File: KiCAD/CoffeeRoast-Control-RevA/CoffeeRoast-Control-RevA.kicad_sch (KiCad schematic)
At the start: 0 parts

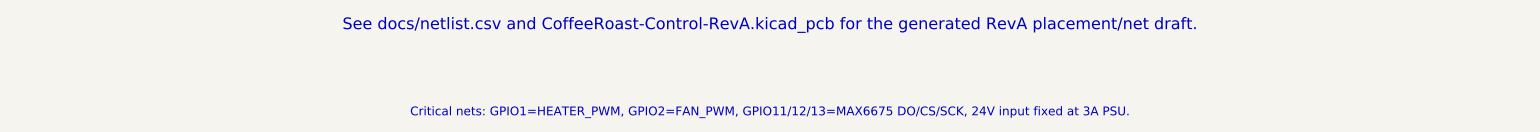
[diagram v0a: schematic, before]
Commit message: Improve CoffeeRoast RevA PCB robustness
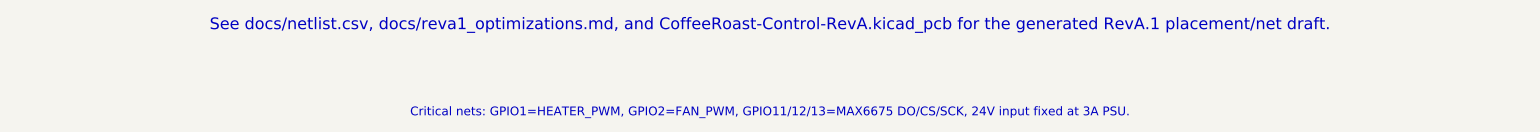
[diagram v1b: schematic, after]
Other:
- note added: "See docs/netlist.csv, docs/reva1_optimizations.md, and CoffeeRoast-Control-RevA.kicad_pcb for the generated RevA.1 placement/net draft."
- note removed: "See docs/netlist.csv and CoffeeRoast-Control-RevA.kicad_pcb for the generated RevA placement/net draft."
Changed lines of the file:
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@@
     (title "CoffeeRoast Control RevA")
     (date "2026-07-04")
-    (rev "A-draft")
+    (rev "A.1-draft")
     (company "CoffeeRoast")
-    (comment 1 "Low-voltage controller PCB: 24V/3A input, 5V buck, 3V3 ESP32-S3-WROOM-1, MAX6675, fan MOSFET, SSR driver")
+    (comment 1 "RevA.1 low-voltage PCB: 24V/3A input, TVS/bulk protection, 5V buck, 3V3 switching regulator, MAX6675, fan MOSFET, SSR driver")
     (comment 2 "230V stays off this PCB: use certified internal 230VAC->24VDC PSU and external SSR module/heatsink")
   )
-  (text "See docs/netlist.csv and CoffeeRoast-Control-RevA.kicad_pcb for the generated RevA placement/net draft." (at 20 30 0) (effects (font (size 2 2))))
+  (text "See docs/netlist.csv, docs/reva1_optimizations.md, and CoffeeRoast-Control-RevA.kicad_pcb for the generated RevA.1 placement/net draft." (at 20 30 0) (effects (font (size 2 2))))
   (text "Critical nets: GPIO1=HEATER_PWM, GPIO2=FAN_PWM, GPIO11/12/13=MAX6675 DO/CS/SCK, 24V input fixed at 3A PSU." (at 20 45 0) (effects (font (size 1.5 1.5))))
   (sheet_instances (path "/" (page "1")))

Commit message: feat: add complete CoffeeRoast KiCad schematic
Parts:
- added C1: 10uF_5V, symbol Device:C
- added C2: 10uF_3V3, symbol Device:C
- added C3: 100nF_MAX6675, symbol Device:C
- added C4: 220uF_35V, symbol Device:C_Polarized
- added C5: 1nF_C0G_DNP_IF_BIASED, symbol Device:C
- added C6: 100nF_U1_DECOUPLING, symbol Device:C
- added C7: 100nF_U4_OUT, symbol Device:C
- added D1: SB560_FLYBACK, symbol Device:D
- added D2: SMBJ33A_INPUT_TVS, symbol Device:D_TVS
- added D3: SMBJ33A_FAN_TVS, symbol Device:D_TVS
- added F1: T3.15A_24V_SIDE, symbol Device:Fuse
- added J1: 24V_IN_FROM_CERTIFIED_PSU, symbol Connector_Generic:Conn_01x02
- added J2: 24V_FAN_OUTPUT, symbol Connector_Generic:Conn_01x02
- added J3: EXTERNAL_SSR_INPUT, symbol Connector_Generic:Conn_01x02
- added J4: K_TYPE_THERMOCOUPLE, symbol Connector_Generic:Conn_01x02
- added J5: USB_C_RECEPTACLE_USB2, Connector_USB:USB_C_Receptacle_XKB_U262-16XN-4BVC11, symbol Connector_Generic:Conn_01x08
- added JGPIO1: SPARE_GPIO_BREAKOUT, symbol Connector_Generic:Conn_01x06
- added Q1: 3V3_LOGIC_NMOS_FAN_GDS, symbol Connector_Generic:Conn_01x03
- added Q2: 2N7002_SSR_DRIVER_GDS, symbol Connector_Generic:Conn_01x03
- added R1, R3: 100R, symbol Device:R
- added R10: 5.1k_CC1_RD, symbol Device:R
- added R11: 5.1k_CC2_RD, symbol Device:R
- added R2, R4: 100k_GATE_PULLDOWN, symbol Device:R
- added R5: 10k_EN_PULLUP, symbol Device:R
- added R6: 10k_BOOT_PULLUP, symbol Device:R
- added R7: 27R_USB_DN, symbol Device:R
- added R8: 27R_USB_DP, symbol Device:R
- added SW1: RESET, symbol Switch:SW_Push
- added SW2: BOOT, symbol Switch:SW_Push
- added TP24V: 24V_FUSED, symbol Connector_Generic:Conn_01x01
- added TP3V3: 3V3, symbol Connector_Generic:Conn_01x01
- added TP5V: 5V, symbol Connector_Generic:Conn_01x01
- added TPBOOT1: BOOT_TWEEZER, symbol Connector_Generic:Conn_01x02
- added TPGND: GND, symbol Connector_Generic:Conn_01x01
- added TPRESET1: RESET_TWEEZER, symbol Connector_Generic:Conn_01x02
- added TPSSR1: SSR_OUT_MEASURE, symbol Connector_Generic:Conn_01x02
- added U1: ESP32-S3-WROOM-1, RF_Module:ESP32-S3-WROOM-1, symbol Connector_Generic:Conn_02x20_Odd_Even
- added U2: MAX6675_SOIC8_3V3, Package_SO:SOIC-8_3.9x4.9mm_P1.27mm, symbol Connector_Generic:Conn_01x08
- added U3: 3V3_SWITCHING_REGULATOR, symbol Connector_Generic:Conn_01x03
- added U4: 24V_TO_5V_BUCK_MODULE, symbol Connector_Generic:Conn_01x04
- added U5: USBLC6-2SC6_USB_ESD, symbol Connector_Generic:Conn_01x06
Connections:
- new net +24V_FUSED: D1.2 (A), D3.1 (A1), F1.2, J2.1 (Pin_1), TP24V.1 (Pin_1), U4.1 (Pin_1)
- new net +24V_RAW: C4.1, D2.1 (A1), F1.1, J1.1 (Pin_1)
- new net +3V3: C2.1, C3.1, C6.1, R5.1, R6.1, TP3V3.1 (Pin_1), U1.2 (Pin_2), U2.4 (Pin_4), U3.2 (Pin_2)
- new net +5V: C1.1, C7.1, J3.1 (Pin_1), TP5V.1 (Pin_1), TPSSR1.1 (Pin_1), U3.3 (Pin_3), U4.3 (Pin_3)
- new net BOOT: R6.2, SW2.1, TPBOOT1.1 (Pin_1), U1.27 (Pin_27)
- new net EN: R5.2, SW1.1, TPRESET1.1 (Pin_1), U1.3 (Pin_3)
- new net FAN_GATE: Q1.1 (Pin_1), R1.2, R2.1
- new net FAN_NEG: D1.1 (K), D3.2 (A2), J2.2 (Pin_2), Q1.2 (Pin_2)
- new net FAN_PWM: R1.1, U1.38 (Pin_38)
- new net GND: C1.2, C2.2, C3.2, C4.2, C6.2, C7.2, D2.2 (A2), J1.2 (Pin_2), J5.1 (Pin_1), J5.8 (Pin_8), Q1.3 (Pin_3), Q2.2 (Pin_2), R10.2, R11.2, R2.2, R4.2, SW1.2, SW2.2, TPBOOT1.2 (Pin_2), TPGND.1 (Pin_1), TPRESET1.2 (Pin_2), U1.1 (Pin_1), U1.40 (Pin_40), U2.1 (Pin_1), U2.8 (Pin_8), U3.1 (Pin_1), U4.2 (Pin_2), U4.4 (Pin_4), U5.3 (Pin_3), U5.4 (Pin_4)
- new net GPIO10: JGPIO1.4 (Pin_4), U1.18 (Pin_18)
- new net GPIO3: JGPIO1.1 (Pin_1), U1.15 (Pin_15)
- new net GPIO45: JGPIO1.6 (Pin_6), U1.26 (Pin_26)
- new net GPIO46: JGPIO1.2 (Pin_2), U1.16 (Pin_16)
- new net GPIO48: JGPIO1.5 (Pin_5), U1.25 (Pin_25)
- new net GPIO9: JGPIO1.3 (Pin_3), U1.17 (Pin_17)
- new net HEATER_PWM: R3.1, U1.39 (Pin_39)
- new net MAX_CS: U1.20 (Pin_20), U2.6 (Pin_6)
- new net MAX_DO: U1.19 (Pin_19), U2.7 (Pin_7)
- new net MAX_SCK: U1.21 (Pin_21), U2.5 (Pin_5)
- new net SSR_GATE: Q2.1 (Pin_1), R3.2, R4.1
- new net SSR_NEG: J3.2 (Pin_2), Q2.3 (Pin_3), TPSSR1.2 (Pin_2)
- new net THERMO_MINUS: C5.2, J4.2 (Pin_2), U2.2 (Pin_2)
- new net THERMO_PLUS: C5.1, J4.1 (Pin_1), U2.3 (Pin_3)
- new net USB_CC1: J5.3 (Pin_3), R10.1
- new net USB_CC2: J5.6 (Pin_6), R11.1
- new net USB_DN: J5.5 (Pin_5), R7.1, U5.1 (Pin_1), U5.6 (Pin_6)
- new net USB_DN_MCU: R7.2, U1.13 (Pin_13)
- new net USB_DP: J5.4 (Pin_4), R8.1, U5.2 (Pin_2), U5.5 (Pin_5)
- new net USB_DP_MCU: R8.2, U1.14 (Pin_14)
- new net USB_VBUS: J5.2 (Pin_2), J5.7 (Pin_7)
- no-connect marks 0 -> 22
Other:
- note added: "230 VAC IS OFF-BOARD: certified 230VAC→24VDC PSU + external SSR/heatsink + thermal cutoff"
- note added: "All named nets here match the routed PCB. Exact U3/U4/U5/Q1/D2/D3 sourced parts remain pre-fabrication review items."
- note added: "BRING-UP / TEST ACCESS"
- note added: "COFFEEROAST CONTROL RevA.1 — LOW-VOLTAGE CONTROLLER"
- note added: "ESP32-S3-WROOM-1 CONTROLLER"
- note added: "FAN + EXTERNAL SSR DRIVERS"
- note added: "Firmware: DO=GPIO11, CS=GPIO12, SCK=GPIO13"
- note added: "K-TYPE THERMOCOUPLE / MAX6675"
- note added: "POWER INPUT / PROTECTION / CONVERSION"
- note added: "SSR input only — no mains on PCB"
- note added: "TPESP1–40 and PADESP1–40 on PCB mirror U1 pins 1–40; see docs/esp32_debug_pads.csv"
- note added: "USB VBUS does not power the controller"
- note added: "USB-C DATA / FLASH (VBUS SENSE ONLY)"
- note removed: "Critical nets: GPIO1=HEATER_PWM, GPIO2=FAN_PWM, GPIO11/12/13=MAX6675 DO/CS/SCK, 24V input fixed at 3A PSU."
- note removed: "See docs/netlist.csv, docs/reva1_optimizations.md, and CoffeeRoast-Control-RevA.kicad_pcb for the generated RevA.1 placement/net draft."
- title: CoffeeRoast Control RevA -> CoffeeRoast Control RevA.1
